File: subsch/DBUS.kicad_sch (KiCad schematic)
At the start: 5 parts

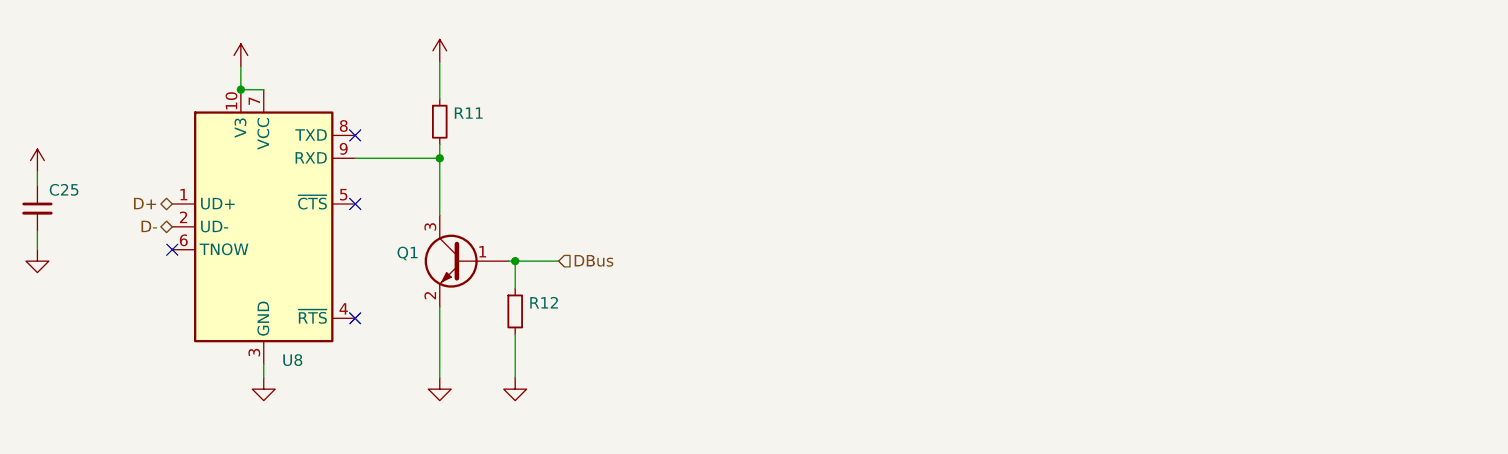
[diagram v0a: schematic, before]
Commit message: Big update on UART-pilot lamp/routings/connectors/esd protection
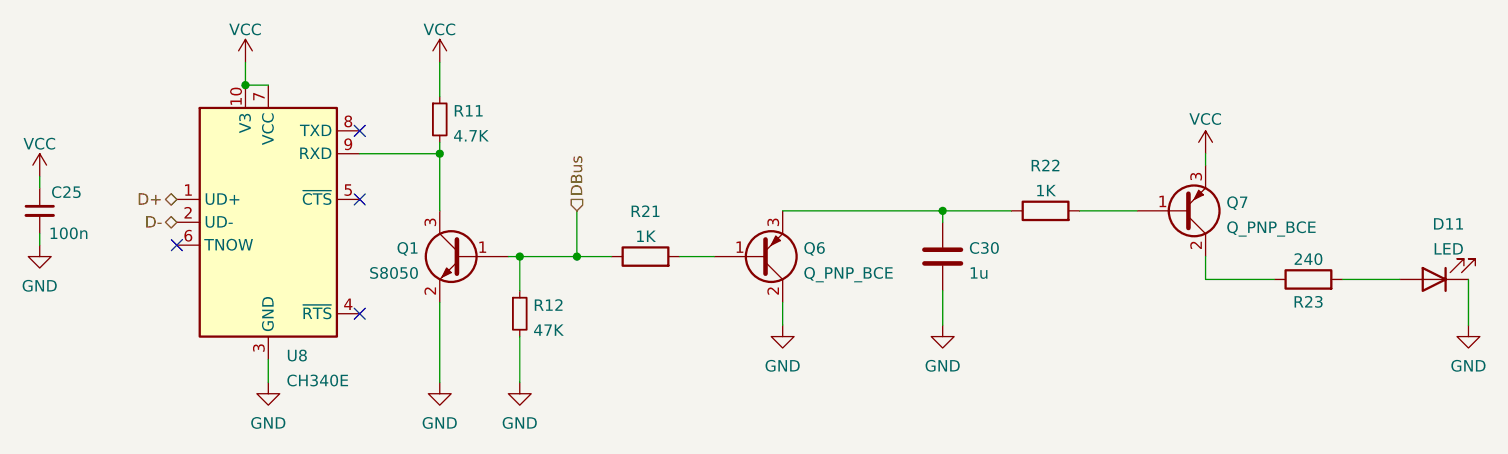
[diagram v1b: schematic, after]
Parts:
- added C30: 1u, Capacitor_SMD:C_0603_1608Metric, symbol Device:C
- added D11: LED, LED_SMD:LED_0603_1608Metric, symbol Device:LED
- added Q6, Q7: Q_PNP_BCE, Package_TO_SOT_SMD:SOT-23, symbol Device:Q_PNP_BCE
- added R21, R22: 1K, Resistor_SMD:R_0603_1608Metric, symbol Device:R
- added R23: 240, Resistor_SMD:R_0603_1608Metric, symbol Device:R
- C25: value (none) -> 100n; footprint (none) -> Capacitor_SMD:C_0603_1608Metric
- Q1: value (none) -> S8050; footprint (none) -> Package_TO_SOT_SMD:SOT-23
- R11: value (none) -> 4.7K; footprint (none) -> Resistor_SMD:R_0603_1608Metric
- R12: value (none) -> 47K; footprint (none) -> Resistor_SMD:R_0603_1608Metric
- U8: value (none) -> CH340E; footprint (none) -> Package_SO:MSOP-10_3x3mm_P0.5mm
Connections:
- net DBus: now also R21.1
- net GND: now also C30.2, D11.1 (K), Q6.2 (C)
- net VCC: now also Q7.3 (E)
- new net: Q7.2 (C), R23.1
- new net: D11.2 (A), R23.2
- new net: C30.1, Q6.3 (E), R22.1
- new net: Q7.1 (B), R22.2
- new net: Q6.1 (B), R21.2
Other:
- moved on the sheet: Q1, R12, U8
